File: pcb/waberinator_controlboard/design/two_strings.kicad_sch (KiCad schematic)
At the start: 13 parts, among them J5 preconf. cable, J6 preconf. cable, J7 Strang A, J8 Strang B, Q2 SISHA04DN-T1-GE3, Q3 SISHA04DN-T1-GE3, U5 MCP14A0304xMNY

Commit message: [HW] draft chassis
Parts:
- added J18, J21: Conn_01x01_Pin, g7_connectors:Chassis_Connector, symbol Connector:Conn_01x01_Pin
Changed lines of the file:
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@@
+    )
+  )
+  (symbol (lib_id "Connector:Conn_01x01_Pin") (at 215.9 92.075 0) (unit 1)
+    (in_bom yes) (on_board yes) (dnp no) (fields_autoplaced)
+    (property "Reference" "J21" (at 216.535 86.995 0)
+      (effects (font (size 1.27 1.27)))
+    )
+    (property "Value" "Conn_01x01_Pin" (at 216.535 89.535 0)
+      (effects (font (size 1.27 1.27)))
+    )
+    (property "Footprint" "g7_connectors:Chassis_Connector" (at 215.9 92.075 0)
+      (effects (font (size 1.27 1.27)) hide)
+    )
+    (property "Datasheet" "~" (at 215.9 92.075 0)
+      (effects (font (size 1.27 1.27)) hide)
+    )
+    (pin "1")
+    (instances
+      (project "Waberinator_hw2"
+        (path "/2abe1fd5-5254-4661-ace0-8064915e9450/6469c7de-d8aa-46cc-834a-51af17622324"
+          (reference "J21") (unit 1)
+        )
+        (path "/2abe1fd5-5254-4661-ace0-8064915e9450/f54d2f9c-99db-4a49-9335-05587a5edeff"
+          (reference "J22") (unit 1)
+        )
+        (path "/2abe1fd5-5254-4661-ace0-8064915e9450/f1caec4a-7324-4287-89c1-78eb5467cd17"
+          (reference "J23") (unit 1)
+        )
+      )
     )
   )
@@
         )
       )
+    )
+  )
+  (symbol (lib_id "Connector:Conn_01x01_Pin") (at 215.9 74.295 0) (unit 1)
+    (in_bom yes) (on_board yes) (dnp no) (fields_autoplaced)
+    (property "Reference" "J18" (at 216.535 69.215 0)
+      (effects (font (size 1.27 1.27)))
+    )
+    (property "Value" "Conn_01x01_Pin" (at 216.535 71.755 0)
+      (effects (font (size 1.27 1.27)))
+    )
+    (property "Footprint" "g7_connectors:Chassis_Connector" (at 215.9 74.295 0)
+      (effects (font (size 1.27 1.27)) hide)
+    )
+    (property "Datasheet" "~" (at 215.9 74.295 0)
+      (effects (font (size 1.27 1.27)) hide)
+    )
+    (pin "1")
+    (instances
+      (project "Waberinator_hw2"
+        (path "/2abe1fd5-5254-4661-ace0-8064915e9450/6469c7de-d8aa-46cc-834a-51af17622324"
+          (reference "J18") (unit 1)
+        )
+        (path "/2abe1fd5-5254-4661-ace0-8064915e9450/f54d2f9c-99db-4a49-9335-05587a5edeff"
+          (reference "J19") (unit 1)
+        )
+        (path "/2abe1fd5-5254-4661-ace0-8064915e9450/f1caec4a-7324-4287-89c1-78eb5467cd17"
+          (reference "J20") (unit 1)
+        )
+      )

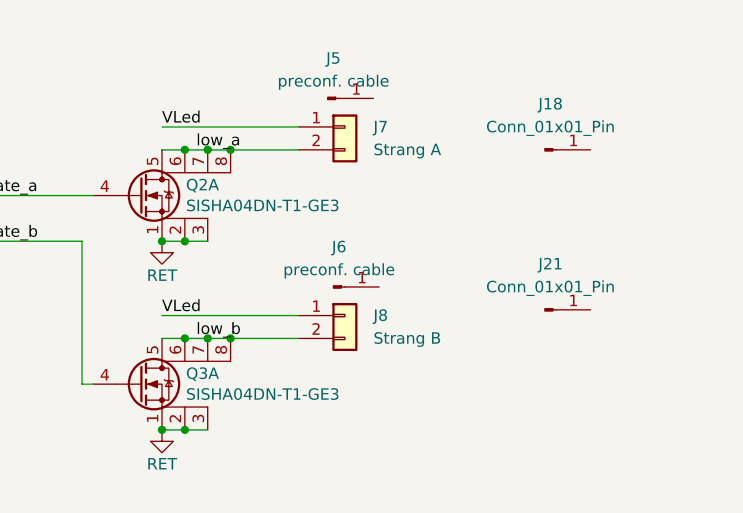
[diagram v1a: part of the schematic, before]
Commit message: [HW] moved lights connector to top
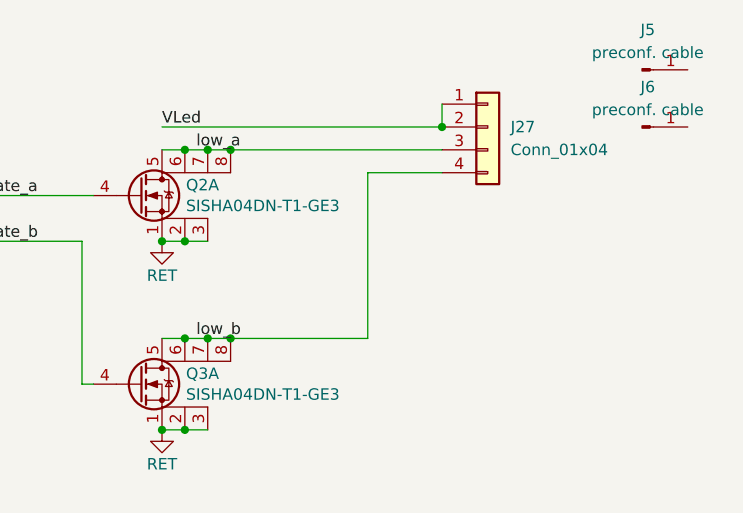
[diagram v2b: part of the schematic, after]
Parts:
- removed J18, J21: Conn_01x01_Pin, g7_connectors:Chassis_Connector, symbol Connector:Conn_01x01_Pin
- removed J7: Strang A, Connector_JST:JST_XH_B2B-XH-AM_1x02_P2.50mm_Vertical, symbol Connector_Generic:Conn_01x02
- removed J8: Strang B, Connector_JST:JST_XH_B2B-XH-AM_1x02_P2.50mm_Vertical, symbol Connector_Generic:Conn_01x02
- added J27: Conn_01x04, Connector_JST:JST_PH_B4B-PH-K_1x04_P2.00mm_Vertical, symbol Connector_Generic:Conn_01x04
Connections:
- net VLED: now also J27.1 (Pin_1), J27.2 (Pin_2)
- net low_a: now also J27.3 (Pin_3)
- net low_b: now also J27.4 (Pin_4)
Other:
- moved on the sheet: J5, J6

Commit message: [HW] Details
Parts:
- R24, R25: footprint Resistor_SMD:R_0603_1608Metric_Pad0.98x0.95mm_HandSolder -> Resistor_SMD:R_0402_1005Metric_Pad0.72x0.64mm_HandSolder
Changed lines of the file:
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@@
       (effects (font (size 1.27 1.27)))
     )
-    (property "Footprint" "Resistor_SMD:R_0603_1608Metric_Pad0.98x0.95mm_HandSolder" (at 114.935 109.728 90)
+    (property "Footprint" "Resistor_SMD:R_0402_1005Metric_Pad0.72x0.64mm_HandSolder" (at 114.935 109.728 90)
       (effects (font (size 1.27 1.27)) hide)
     )
@@
       (effects (font (size 1.27 1.27)))
     )
-    (property "Footprint" "Resistor_SMD:R_0603_1608Metric_Pad0.98x0.95mm_HandSolder" (at 114.935 115.443 90)
-      (effects (font (size 1.27 1.27)) hide)
-    )
+    (property "Footprint" "Resistor_SMD:R_0402_1005Metric_Pad0.72x0.64mm_HandSolder" (at 114.935 115.443 90)
+      (effects (font (size 1.27 1.27)) hide)
+    )

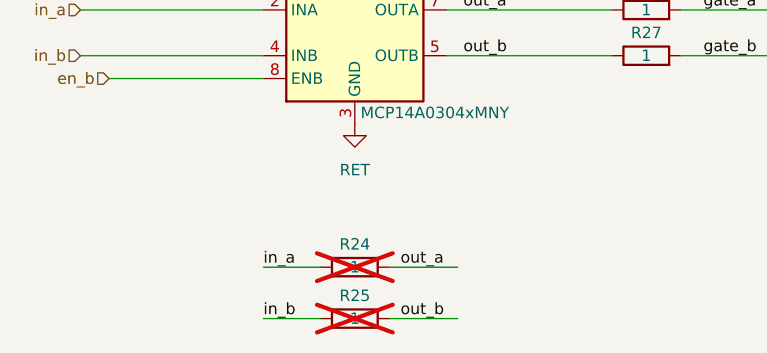
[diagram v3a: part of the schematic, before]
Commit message: [HW] pcb production ready
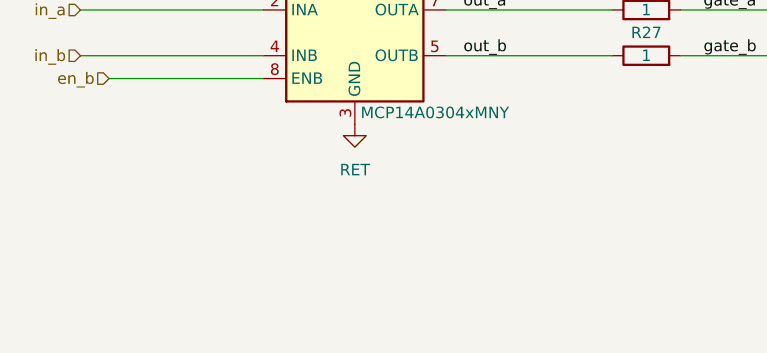
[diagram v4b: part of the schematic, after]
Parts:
- removed R24, R25: 1, Resistor_SMD:R_0402_1005Metric_Pad0.72x0.64mm_HandSolder, symbol Device:R
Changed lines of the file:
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@@
-    (stroke (width 0) (type default))
-  )
-  (wire (pts (xy 104.775 113.665) (xy 111.125 113.665))
-    (stroke (width 0) (type default))
-  )
-  (wire (pts (xy 118.745 107.95) (xy 126.365 107.95))
-    (stroke (width 0) (type default))
-  )
-  (wire (pts (xy 118.745 113.665) (xy 126.365 113.665))
-    (stroke (width 0) (type default))
-  )
-  (wire (pts (xy 104.775 107.95) (xy 111.125 107.95))
     (stroke (width 0) (type default))
   )
@@
     (effects (font (size 1.27 1.27)) (justify left bottom))
   )
-  (label "out_b" (at 120.015 113.665 0) (fields_autoplaced)
-    (effects (font (size 1.27 1.27)) (justify left bottom))
-  )
   (label "VLed" (at 173.355 71.755 0) (fields_autoplaced)
     (effects (font (size 1.27 1.27)) (justify left bottom))
   )
-  (label "in_b" (at 104.775 113.665 0) (fields_autoplaced)
-    (effects (font (size 1.27 1.27)) (justify left bottom))
-  )
   (label "gate_a" (at 153.67 79.375 0) (fields_autoplaced)
     (effects (font (size 1.27 1.27)) (justify left bottom))
@@
     (effects (font (size 1.27 1.27)) (justify left bottom))
   )
-  (label "out_a" (at 120.015 107.95 0) (fields_autoplaced)
-    (effects (font (size 1.27 1.27)) (justify left bottom))
-  )
-  (label "in_a" (at 104.775 107.95 0) (fields_autoplaced)
-    (effects (font (size 1.27 1.27)) (justify left bottom))
-  )
   (hierarchical_label "en_b" (shape input) (at 87.63 86.995 180) (fields_autoplaced)
     (effects (font (size 1.27 1.27)) (justify right))
@@
   (hierarchical_label "in_b" (shape input) (at 84.455 84.455 180) (fields_autoplaced)
     (effects (font (size 1.27 1.27)) (justify right))
-  )
-  (symbol (lib_id "Device:R") (at 114.935 107.95 90) (unit 1)
-    (in_bom yes) (on_board yes) (dnp yes)
-    (property "Reference" "R24" (at 114.935 105.41 90)
-      (effects (font (size 1.27 1.27)))
-    )
-    (property "Value" "1" (at 114.935 107.95 90)
-      (effects (font (size 1.27 1.27)))
-    )
-    (property "Footprint" "Resistor_SMD:R_0402_1005Metric_Pad0.72x0.64mm_HandSolder" (at 114.935 109.728 90)
-      (effects (font (size 1.27 1.27)) hide)
-    )
-    (property "Datasheet" "~" (at 114.935 107.95 0)
-      (effects (font (size 1.27 1.27)) hide)
-    )
-    (pin "2")
-    (pin "1")
-    (instances
-      (project "Waberinator_hw2"
-        (path "/2abe1fd5-5254-4661-ace0-8064915e9450/6469c7de-d8aa-46cc-834a-51af17622324"
-          (reference "R24") (unit 1)
-        )
-        (path "/2abe1fd5-5254-4661-ace0-8064915e9450/f1caec4a-7324-4287-89c1-78eb5467cd17"
-          (reference "R32") (unit 1)
-        )
-        (path "/2abe1fd5-5254-4661-ace0-8064915e9450/f54d2f9c-99db-4a49-9335-05587a5edeff"
-          (reference "R28") (unit 1)
-        )
-      )
-    )
   )
   (symbol (lib_id "Connector:Conn_01x01_Pin") (at 226.695 65.405 0) (unit 1)
@@
         )
       )
-    )
-  )
-  (symbol (lib_id "Device:R") (at 114.935 113.665 90) (unit 1)
-    (in_bom yes) (on_board yes) (dnp yes)
-    (property "Reference" "R25" (at 114.935 111.125 90)
-      (effects (font (size 1.27 1.27)))
-    )
-    (property "Value" "1" (at 114.935 113.665 90)
-      (effects (font (size 1.27 1.27)))
-    )
-    (property "Footprint" "Resistor_SMD:R_0402_1005Metric_Pad0.72x0.64mm_HandSolder" (at 114.935 115.443 90)
-      (effects (font (size 1.27 1.27)) hide)
-    )
-    (property "Datasheet" "~" (at 114.935 113.665 0)
-      (effects (font (size 1.27 1.27)) hide)
-    )
-    (pin "2")
-    (pin "1")
-    (instances
-      (project "Waberinator_hw2"
-        (path "/2abe1fd5-5254-4661-ace0-8064915e9450/6469c7de-d8aa-46cc-834a-51af17622324"
-          (reference "R25") (unit 1)
-        )
-        (path "/2abe1fd5-5254-4661-ace0-8064915e9450/f1caec4a-7324-4287-89c1-78eb5467cd17"
-          (reference "R33") (unit 1)
-        )
-        (path "/2abe1fd5-5254-4661-ace0-8064915e9450/f54d2f9c-99db-4a49-9335-05587a5edeff"
-          (reference "R29") (unit 1)
-        )
-      )

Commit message: [HW] finish layout
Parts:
- Q2: Digikey SISHA04DN-T1-GE3TR-ND -> SISHA04DN-T1-GE3CT-ND
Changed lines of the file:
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@@
       (effects (font (size 1.27 1.27)) hide)
     )
-    (property "Digikey" "SISHA04DN-T1-GE3TR-ND" (at 170.815 79.375 0)
+    (property "Digikey" "SISHA04DN-T1-GE3CT-ND" (at 170.815 79.375 0)
       (effects (font (size 1.27 1.27)) hide)
     )

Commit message: [HW] misc adjustments to mechanics
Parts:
- J27: Digikey Part Number 455-B4B-XH-A-ND -> 455-1164-ND
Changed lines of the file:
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@@
       (effects (font (size 1.27 1.27)) hide)
     )
-    (property "Digikey Part Number" "455-B4B-XH-A-ND" (at 209.55 71.755 0)
+    (property "Digikey Part Number" "455-1164-ND" (at 209.55 71.755 0)
       (effects (font (size 1.27 1.27)) hide)
     )

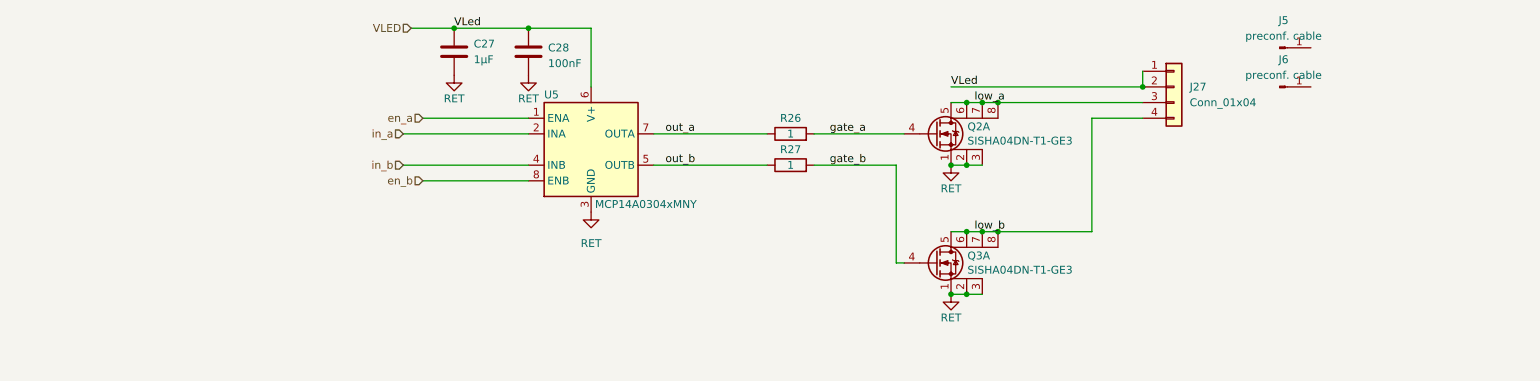
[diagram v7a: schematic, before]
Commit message: feat(cableplan): add rudimentary cableplan to driver schematic sheet
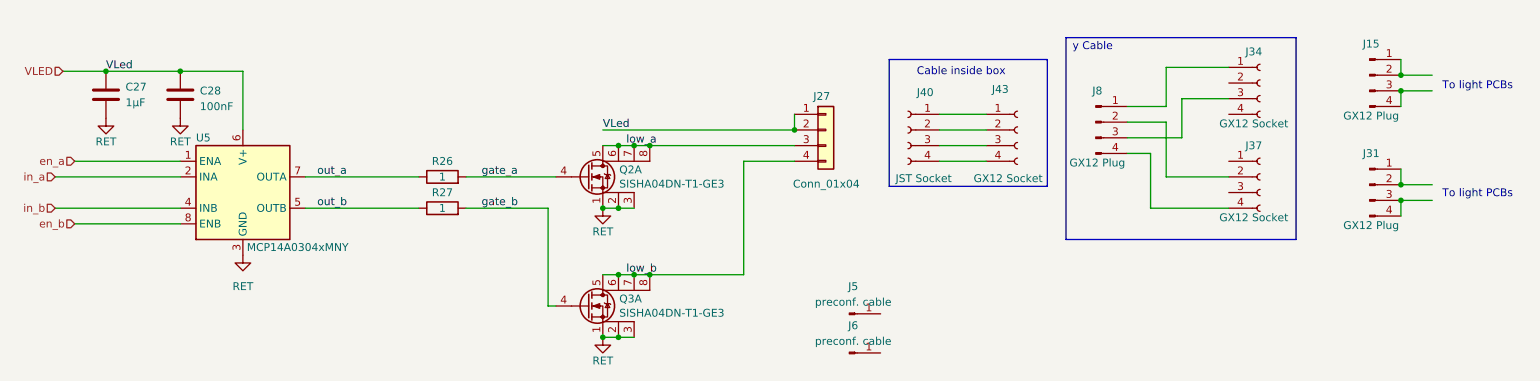
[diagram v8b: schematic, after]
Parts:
- added J15, J31, J8: GX12 Plug, symbol Connector:Conn_01x04_Pin
- added J34, J37, J43: GX12 Socket, symbol Connector:Conn_01x04_Socket
- added J40: JST Socket, symbol Connector:Conn_01x04_Socket
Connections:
- new net: J31.1 (Pin_1), J31.2 (Pin_2)
- new net: J31.3 (Pin_3), J31.4 (Pin_4)
- new net: J40.1 (Pin_1), J43.1 (Pin_1)
- new net: J40.2 (Pin_2), J43.2 (Pin_2)
- new net: J40.3 (Pin_3), J43.3 (Pin_3)
- new net: J40.4 (Pin_4), J43.4 (Pin_4)
- new net: J37.2 (Pin_2), J8.2 (Pin_2)
- new net: J37.4 (Pin_4), J8.4 (Pin_4)
- new net: J34.1 (Pin_1), J8.1 (Pin_1)
- new net: J34.3 (Pin_3), J8.3 (Pin_3)
- new net: J15.1 (Pin_1), J15.2 (Pin_2)
- new net: J15.3 (Pin_3), J15.4 (Pin_4)
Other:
- note added: "Cable inside box"
- note added: "To light PCBs"
- note added: "y Cable"
- moved on the sheet: C27, C28, J27, J5, J6, Q2A, Q3A, R26, R27, U5
